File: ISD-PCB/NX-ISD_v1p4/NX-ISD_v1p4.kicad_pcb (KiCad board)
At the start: 4 copper layers, 77 x 48.6 mm, 113 parts, among them J1 UJ20-C-H-G-SMT-1-P16-TR, J2 1-2328702-0, J3 1051620001, P1 S2B-PH-SM4-TB, Q1 BC847W, Q2 AO3401A, Q3 AO3400A, Q4 AO3400A, U1 RT9193-18GB, U10 OPT3001DNPR, U11 BNO085, U12 RV-3028-C7, U13 ESP32-S3-WROOM-1-N16R8, U2 USBLC6-2P6, U3 TLV62568DBV, U5 BQ25170DSGR, U6 MAX17048G_T10, U7 BME690, U8 MAX30102, U9 PCA9306, Y1 32.768 kHz

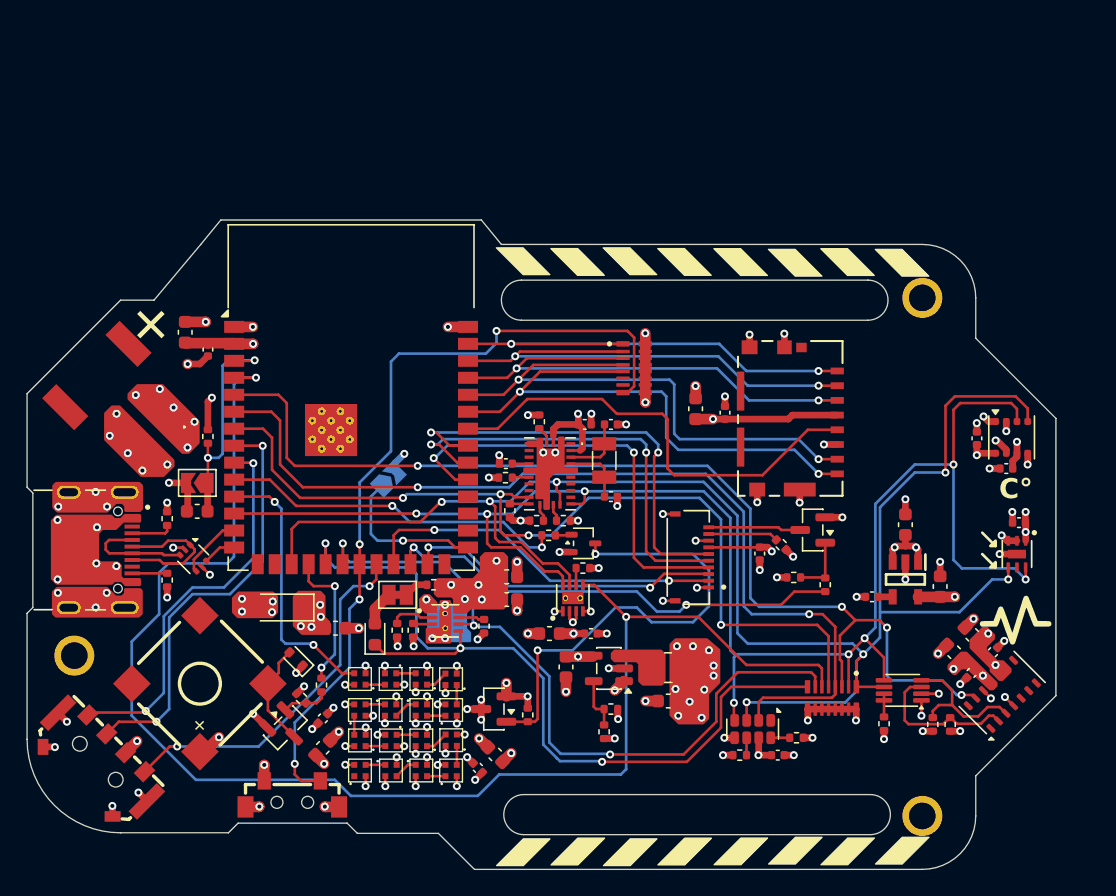
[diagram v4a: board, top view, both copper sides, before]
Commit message: hw(v1.4): complete overall layout plating, esp32 thermal pad, npm silkscreen, and docs
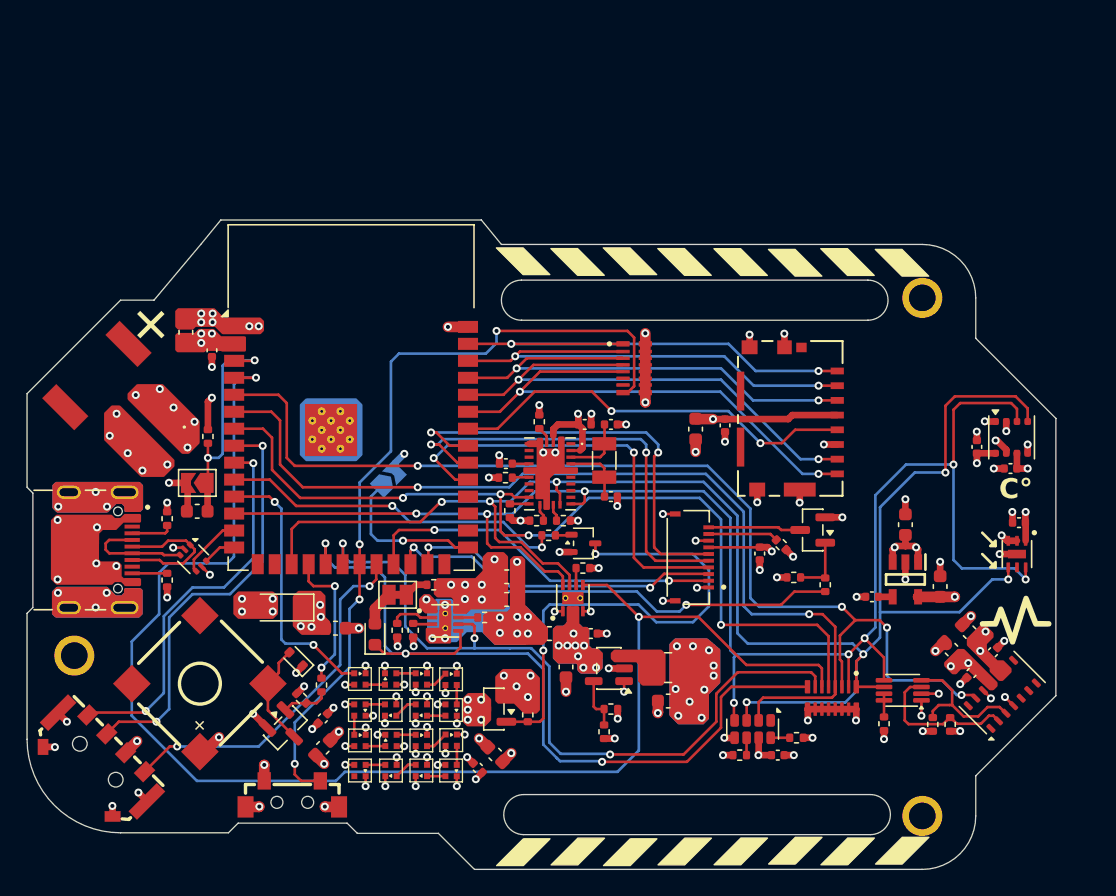
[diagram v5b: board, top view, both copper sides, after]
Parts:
- moved C27 1.53 mm to (162.4, 93.8), turned to -90 degrees
- moved C28 0.95 mm to (164.6, 93.5), turned to -90 degrees
- moved R5 0.65 mm to (146.6, 107.8), turned to 180 degrees
- moved C13 0.64 mm to (183.4, 95.1)
- moved C12 0.32 mm to (186.0, 96.7)
- moved C25 0.30 mm to (126.2, 87.8)
- moved C32 0.28 mm to (181.6, 110.2)
- moved C33 0.28 mm to (182.9, 109.0)
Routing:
- net VBAT: track 12.5 -> 0.84 mm, vias 16 -> 24
- net GND: track 88.9 -> 80.9 mm, vias 112 -> 119
- net +3V3: track 63.6 -> 58.1 mm, vias 38 -> 39
- net /Logic section/SD_CLK: track 34.5 -> 30.8 mm, vias 0 -> 2
- net /Logic section/USB_DETECT: track 54.2 -> 57.2 mm
- net VN: track 15.4 -> 12.9 mm, vias 23 -> 25
- net /Logic section/SD_DAT0: track 41.0 -> 38.8 mm
- net Net-(Q1-C): track 35.2 -> 37.1 mm
- net /Logic section/SD_DAT1: track 41.0 -> 39.1 mm
- net /Logic section/!ALERT: track 107.6 -> 106.8 mm
- net /Logic section/BAT_STAT: track 62.5 -> 63.2 mm
- net Net-(U5-VSET): track 1.97 -> 1.44 mm

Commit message: feat(v1.4): finalize v1.4 PCB, KiCad libraries, production guide, and firmware target selector
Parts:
- added G***: LOGO, NX-ISD_silkscreen designs:SD_card_symbol, F.Cu at (177.2, 93.0)
- moved ? 0.06 mm to (179.4, 84.0)
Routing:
- net +3V3: vias 39 -> 42
- net /Power section/USB_P: vias 10 -> 18
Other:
- board text added: "JLCPCB production settings: Additional settings after uploading the .zip gerber folder: PCB-Thickness: 1.2mm (I personally recommand staying between 1.2mm and 1.6mm) Material Type: FR4-TG155 (Important!) Surface finish: ENIG (Essential for these small pads) Gold Thickness: 1 U{dblquote} Min via hole size/diameter: 0.3mm/(0.4/0.45mm) Optional settings you might want: PCB Color: Black (to your wish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"
- board text removed: "JLCPCB production settings: Additional settings after uploading the .zip gerber folder: PCB-Thickness: 1.2mm (I personally recommand staying between 1.2mm and 1.6mm) Material Type: FR4-TG155 (Important!) Surface finish: ENIG (Essential for these small pads) Gold Thickness: 1 U{dblquote} Min via hole size/diameter: 0.25mm/(0.35/0.4mm) (4-Kelvin test should be automatically selected) Optional setti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"

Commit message: feat(v1.4): update PCB layout with BNO085 3V3 polygon, RTC cap fix, BQ25170 thermal relief, and silkscreen artwork
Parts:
- moved R28 1.10 mm to (164.6, 118.2)
- moved C20 0.95 mm to (167.6, 118.2)
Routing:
- net +3V3: track 58.1 -> 52.0 mm
- net /Logic section/BAT_STAT: track 63.2 -> 63.9 mm
- net Net-(U12-VBACKUP): track 1.30 -> 2.00 mm
- net VBAT: vias 24 -> 25
- net GND: vias 119 -> 120
- net /Power section/USB_P: vias 18 -> 23
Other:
- board text added: "1"
- board text added: "2"
- board text added: "3"
- board text added: "4"
- board text added: "PUT THAT BACK!"
